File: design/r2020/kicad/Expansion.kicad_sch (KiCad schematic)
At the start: 32 parts, among them IC7 74LS148, J3 Conn_02x32_Odd_Even, J3-X1 Conn_01x04_Male, J5 PWR, J6 Conn_01x04_Male

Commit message: More cleanup
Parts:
- removed R12, R15, R17, R18: 4K7, rosco_m68k:0207_10, symbol Device:R

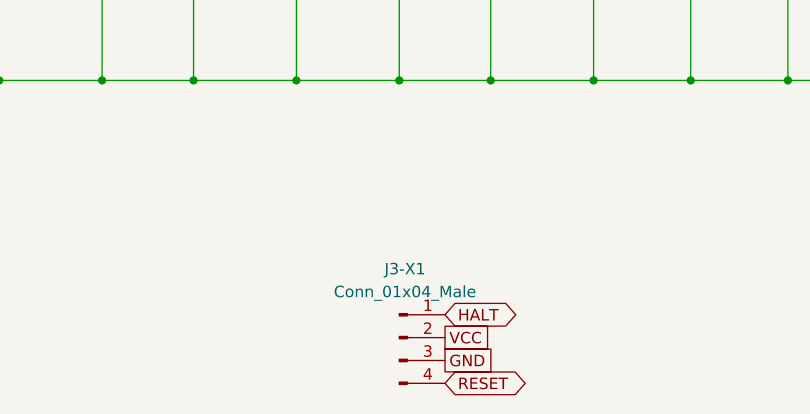
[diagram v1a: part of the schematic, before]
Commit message: Chore/merge 2.42 release master (#403)
* Feture/release 2.4 roll develop (#369)

* Roll 2.4 release

* Roll 2.5.dev

* Roll 2.5.dev release (#370)

* ignore files/dirs starting with dot, tweak prompt

* Ignore static libs

* ROM kernel: initial integration

* Add FW tests to CI

* Add <vector> include

* 🤷 Try fix GITHUB_WORKSPACE thing [3]

* Revert "🤷 Try fix GITHUB_WORKSPACE thing [3]"

This reverts commit 4369599145c125a8a3ae4daa409131a3e2088630.

* Revert "Add FW tests to CI"

This reverts commit 4073f7178b6fe7a046a48ebc25fbea2ce17a4f9d.

* Test in CI, take 2 🤞

* Include user.mk

* Make program responsible for pmm setup

* Change usgae message

* Don't use impl-reserved ids

* Flush all read/writes to stdio

* Cleanup Outdated Equates (#377)

* Remove equates.S

* Remove revision-specific defines from public
Except for MFP, which is the only place that IOBASE was actually used

* Fix comment about equates.S

* Delete firmware attic (#379)

* Fix #359 (#378)

* Feature/gdb lib (#381)

* Add GDB remote debugging support as a library

* Us FSINFO hints

* Fix outdated IC14 reference (#384)

* Fix outdated IC14 reference
* Use reference instead of hardcoding

* Update README.md (#386)

* Feature/68000 probe support (#387)

* Support device probes on 68000

* Switch default CPU to 68000

* Disable memcheck on 68000

* Don't (ab)use SDB_STATUS for BERR_HANDLER return

* Replace nasty label address hack

* Consistently use INSTALL_TEMP_BERR_HANDLER

* Update typos in documentation

* Fix SD Card write failures by increasing timeout

* Feature/kicad 7 (#388)

* Update r2 to Kicad 7
* Update r2020 to Kicad 7
* Complete Kicad 7 migration

* Update README.md

* Feature/swap tx rx again (#395)

* Swap TX/RX & CTS/RTS silkscreen r2

* Swap over labels
* Add arrows
* Some board tidy up

* Swap TX/RX & CTS/RTS silkscreen r2020

    * Swap over labels
    * Add arrows
    *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
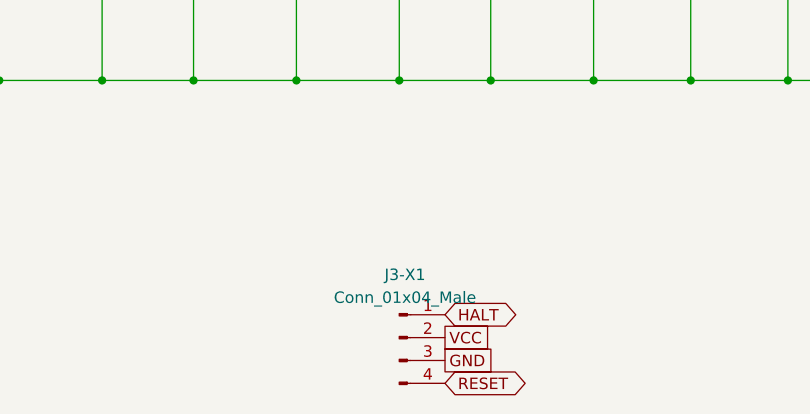
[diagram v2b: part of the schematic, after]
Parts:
- J3-X1, J6: symbol Connector:Conn_01x04_Male -> Connector:Conn_01x04_Pin

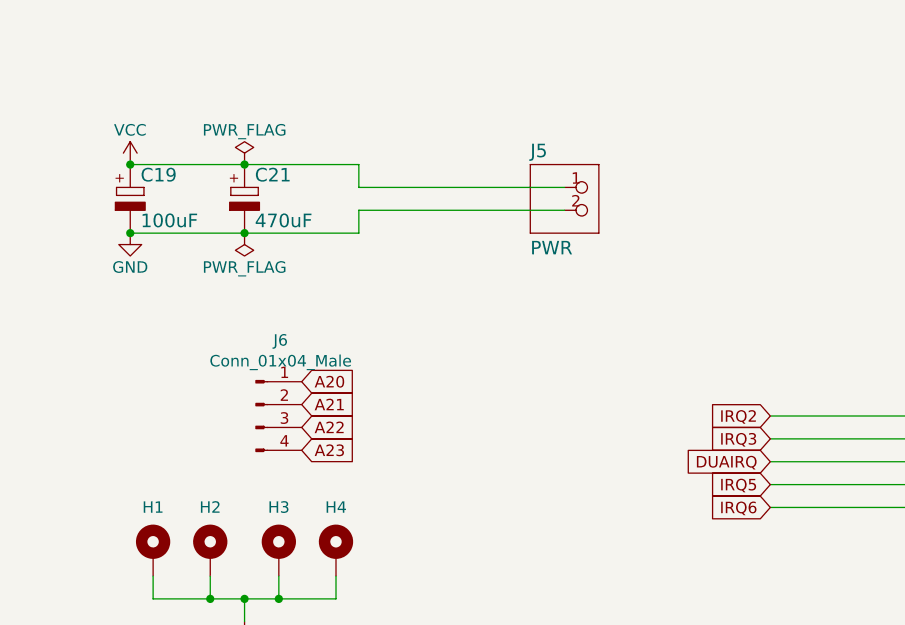
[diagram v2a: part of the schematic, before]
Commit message: Minor classic refresh for 2024 (#416)
* Minor classic refresh for 2024

* Add DC jack
* Silk cleanup
* Unify added memory expansion headers
* Minor routing cleanup
* QR code on silk

* Fix 2020 missing polarity symbol
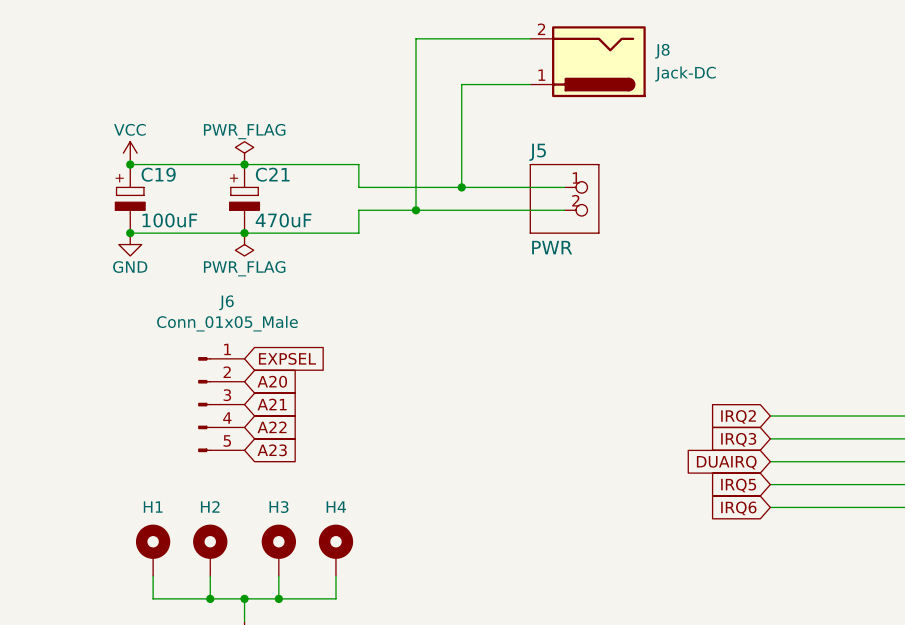
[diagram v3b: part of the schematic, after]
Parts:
- removed J6: Conn_01x04_Male, Connector_PinHeader_2.54mm:PinHeader_1x04_P2.54mm_Vertical, symbol Connector:Conn_01x04_Pin
- added J6: Conn_01x05_Male, Connector_PinHeader_2.54mm:PinHeader_1x05_P2.54mm_Vertical, symbol Connector:Conn_01x05_Pin
- added J8: Jack-DC, Connector_BarrelJack:BarrelJack_Horizontal, symbol Connector:Jack-DC
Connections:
- net A20: now also J6.2 (Pin_2)
- net A21: now also J6.3 (Pin_3)
- net A22: now also J6.4 (Pin_4)
- net A23: now also J6.5 (Pin_5)
- net EXPSEL: now also J6.1 (Pin_1)
- net GND: now also J8.2
- net VCC: now also J8.1
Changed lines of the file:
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@@
   (junction (at 106.68 118.11) (diameter 0) (color 0 0 0 0)
   )
+  (junction (at 60.96 40.64) (diameter 0) (color 0 0 0 0)
+  )
   (junction (at 73.66 118.11) (diameter 0) (color 0 0 0 0)
   )
@@
   )
   (junction (at 45.72 83.82) (diameter 0) (color 0 0 0 0)
+  )
+  (junction (at 66.04 38.1) (diameter 0) (color 0 0 0 0)
   )
   (junction (at 119.38 50.8) (diameter 0) (color 0 0 0 0)
@@
     (stroke (width 0) (type default))
   )
+  (wire (pts (xy 66.04 26.67) (xy 66.04 38.1))
+    (stroke (width 0) (type default))
+  )
   (wire (pts (xy 106.68 135.89) (xy 106.68 146.05))
     (stroke (width 0) (type default))
@@
     (stroke (width 0) (type default))
   )
+  (wire (pts (xy 66.04 38.1) (xy 54.61 38.1))
+    (stroke (width 0) (type default))
+  )
   (wire (pts (xy 73.66 146.05) (xy 85.09 146.05))
     (stroke (width 0) (type default))
@@
     (stroke (width 0) (type default))
   )
-  (wire (pts (xy 77.47 38.1) (xy 54.61 38.1))
+  (wire (pts (xy 77.47 38.1) (xy 66.04 38.1))
+    (stroke (width 0) (type default))
+  )
+  (wire (pts (xy 60.96 21.59) (xy 60.96 40.64))
     (stroke (width 0) (type default))
   )
@@
     (stroke (width 0) (type default))
   )
-  (wire (pts (xy 77.47 40.64) (xy 54.61 40.64))
+  (wire (pts (xy 77.47 40.64) (xy 60.96 40.64))
     (stroke (width 0) (type default))
   )
@@
     (stroke (width 0) (type default))
   )
+  (wire (pts (xy 60.96 40.64) (xy 54.61 40.64))
+    (stroke (width 0) (type default))
+  )
   (wire (pts (xy 73.66 118.11) (xy 62.23 118.11))
     (stroke (width 0) (type default))
@@
     (stroke (width 0) (type default))
   )
+  (wire (pts (xy 73.66 21.59) (xy 60.96 21.59))
+    (stroke (width 0) (type default))
+  )
   (wire (pts (xy 100.33 73.66) (xy 148.59 73.66))
     (stroke (width 0) (type default))
@@
     (stroke (width 0) (type default))
   )
+  (wire (pts (xy 73.66 26.67) (xy 66.04 26.67))
+    (stroke (width 0) (type default))
+  )
   (wire (pts (xy 85.09 135.89) (xy 85.09 146.05))
     (stroke (width 0) (type default))
@@
     (property "Intersheetrefs" "${INTERSHEET_REFS}" (at 0 0 0)
       (effects (font (size 1.27 1.27)) hide)
+    )
+  )
+  (global_label "A20" (shape input) (at 41.91 59.69 0) (fields_autoplaced)
+    (effects (font (size 1.27 1.27)) (justify left))
+    (property "Intersheetrefs" "${INTERSHEET_REFS}" (at 47.7486 59.69 0)
+      (effects (font (size 1.27 1.27)) (justify left) hide)
     )
   )
@@
     )
   )
-  (global_label "A21" (shape input) (at 48.26 62.23 0) (fields_autoplaced)
-    (effects (font (size 1.27 1.27)) (justify left))
-    (property "Intersheetrefs" "${INTERSHEET_REFS}" (at 0 0 0)
-      (effects (font (size 1.27 1.27)) hide)
+  (global_label "A23" (shape input) (at 41.91 67.31 0) (fields_autoplaced)
+    (effects (font (size 1.27 1.27)) (justify left))
+    (property "Intersheetrefs" "${INTERSHEET_REFS}" (at 47.7486 67.31 0)
+      (effects (font (size 1.27 1.27)) (justify left) hide)
     )
   )
@@
     )
   )
+  (global_label "A21" (shape input) (at 41.91 62.23 0) (fields_autoplaced)
+    (effects (font (size 1.27 1.27)) (justify left))
+    (property "Intersheetrefs" "${INTERSHEET_REFS}" (at 47.7486 62.23 0)
+      (effects (font (size 1.27 1.27)) (justify left) hide)
+    )
+  )
   (global_label "A2" (shape input) (at 214.63 45.72 180) (fields_autoplaced)
     (effects (font (size 1.27 1.27)) (justify right))
@@
     )
   )
+  (global_label "A22" (shape input) (at 41.91 64.77 0) (fields_autoplaced)
+    (effects (font (size 1.27 1.27)) (justify left))
+    (property "Intersheetrefs" "${INTERSHEET_REFS}" (at 47.7486 64.77 0)
+      (effects (font (size 1.27 1.27)) (justify left) hide)
+    )
+  )
   (global_label "IPL1" (shape output) (at 173.99 60.96 0) (fields_autoplaced)
     (effects (font (size 1.27 1.27)) (justify left))
@@
     )
   )
-  (global_label "A20" (shape input) (at 48.26 59.69 0) (fields_autoplaced)
-    (effects (font (size 1.27 1.27)) (justify left))
-    (property "Intersheetrefs" "${INTERSHEET_REFS}" (at 0 0 0)
-      (effects (font (size 1.27 1.27)) hide)
-    )
-  )
   (global_label "EXPSEL" (shape output) (at 227.33 63.5 0) (fields_autoplaced)
     (effects (font (size 1.1938 1.1938)) (justify left))
@@
     )
   )
-  (global_label "A22" (shape input) (at 48.26 64.77 0) (fields_autoplaced)
-    (effects (font (size 1.27 1.27)) (justify left))
-    (property "Intersheetrefs" "${INTERSHEET_REFS}" (at 0 0 0)
-      (effects (font (size 1.27 1.27)) hide)
-    )
-  )
   (global_label "D13" (shape bidirectional) (at 227.33 93.98 0) (fields_autoplaced)
     (effects (font (size 1.27 1.27)) (justify left))
@@
     )
   )
+  (global_label "EXPSEL" (shape input) (at 41.91 57.15 0) (fields_autoplaced)
+    (effects (font (size 1.27 1.27)) (justify left))
+    (property "Intersheetrefs" "${INTERSHEET_REFS}" (at 51.2561 57.15 0)
+      (effects (font (size 1.27 1.27)) (justify left) hide)
+    )
+  )
   (global_label "RESET" (shape bidirectional) (at 227.33 86.36 0) (fields_autoplaced)
     (effects (font (size 1.1938 1.1938)) (justify left))
@@
   )
   (global_label "VPA" (shape input) (at 247.65 50.8 0) (fields_autoplaced)
-    (effects (font (size 1.27 1.27)) (justify left))
-    (property "Intersheetrefs" "${INTERSHEET_REFS}" (at 0 0 0)
-      (effects (font (size 1.27 1.27)) hide)
-    )
-  )
-  (global_label "A23" (shape input) (at 48.26 67.31 0) (fields_autoplaced)
     (effects (font (size 1.27 1.27)) (justify left))
     (property "Intersheetrefs" "${INTERSHEET_REFS}" (at 0 0 0)
@@
     )
   )
-  (symbol (lib_id "Connector:Conn_01x04_Pin") (at 43.18 62.23 0) (unit 1)
-    (in_bom yes) (on_board yes) (dnp no)
-    (property "Reference" "J6" (at 45.9232 55.0926 0)
-      (effects (font (size 1.27 1.27)))
-    )
-    (property "Value" "Conn_01x04_Male" (at 45.9232 57.404 0)
-      (effects (font (size 1.27 1.27)))
-    )
-    (property "Footprint" "Connector_PinHeader_2.54mm:PinHeader_1x04_P2.54mm_Vertical" (at 43.18 62.23 0)
-      (effects (font (size 1.27 1.27)) hide)
-    )
-    (property "Datasheet" "~" (at 43.18 62.23 0)
-      (effects (font (size 1.27 1.27)) hide)
-    )
-    (pin "1")
-    (pin "2")
-    (pin "3")
-    (pin "4")
-    (instances
-      (project "rosco_m68k"
-        (path "/9031bb33-c6aa-4758-bf5c-3274ed3ebab7/00000000-0000-0000-0000-00005e53bc83"
-          (reference "J6") (unit 1)
-        )
-      )
-    )
-  )
   (symbol (lib_id "74xx:74LS148") (at 161.29 68.58 0) (unit 1)
     (in_bom yes) (on_board yes) (dnp no)
@@
     )
   )
+  (symbol (lib_id "Connector:Jack-DC") (at 81.28 24.13 180) (unit 1)
+    (in_bom yes) (on_board yes) (dnp no) (fields_autoplaced)
+    (property "Reference" "J8" (at 87.63 22.86 0)
+      (effects (font (size 1.27 1.27)) (justify right))
+    )
+    (property "Value" "Jack-DC" (at 87.63 25.4 0)
+      (effects (font (size 1.27 1.27)) (justify right))
+    )
+    (property "Footprint" "Connector_BarrelJack:BarrelJack_Horizontal" (at 80.01 23.114 0)
+      (effects (font (size 1.27 1.27)) hide)
+    )
+    (property "Datasheet" "~" (at 80.01 23.114 0)
+      (effects (font (size 1.27 1.27)) hide)
+    )
+    (pin "1")
+    (pin "2")
+    (instances
+      (project "rosco_m68k"
+        (path "/9031bb33-c6aa-4758-bf5c-3274ed3ebab7/00000000-0000-0000-0000-00005e53bc83"
+          (reference "J8") (unit 1)
+        )
+      )
+      (project "rosco_6502"
+        (path "/e63e39d7-6ac0-4ffd-8aa3-1841a4541b55"
+          (reference "J7") (unit 1)
+        )
+      )
+    )
+  )
   (symbol (lib_id "rosco_m68k-eagle-import:C2,5-3") (at 162.56 130.81 0) (unit 1)
     (in_bom yes) (on_board yes) (dnp no)
@@
         )
       )
+    )
+  )
+  (symbol (lib_id "Connector:Conn_01x05_Pin") (at 36.83 62.23 0) (unit 1)
+    (in_bom yes) (on_board yes) (dnp no)
+    (property "Reference" "J6" (at 40.005 50.8 0)
+      (effects (font (size 1.27 1.27)))
+    )
+    (property "Value" "Conn_01x05_Male" (at 40.005 53.1114 0)
+      (effects (font (size 1.27 1.27)))
+    )
+    (property "Footprint" "Connector_PinHeader_2.54mm:PinHeader_1x05_P2.54mm_Vertical" (at 36.83 62.23 0)
+      (effects (font (size 1.27 1.27)) hide)
+    )
+    (property "Datasheet" "~" (at 36.83 62.23 0)
+      (effects (font (size 1.27 1.27)) hide)
+    )
+    (pin "1")
+    (pin "2")
+    (pin "3")
+    (pin "4")
+    (pin "5")
+    (instances
+      (project "rosco_m68k"
+        (path "/9031bb33-c6aa-4758-bf5c-3274ed3ebab7/00000000-0000-0000-0000-00005e53bc83"
+          (reference "J6") (unit 1)
+        )
+      )
